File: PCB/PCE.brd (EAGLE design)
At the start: 58.5 x 61 mm, 13 parts, among them U1 SN74AHCT125N, U2 SN74AHCT125N

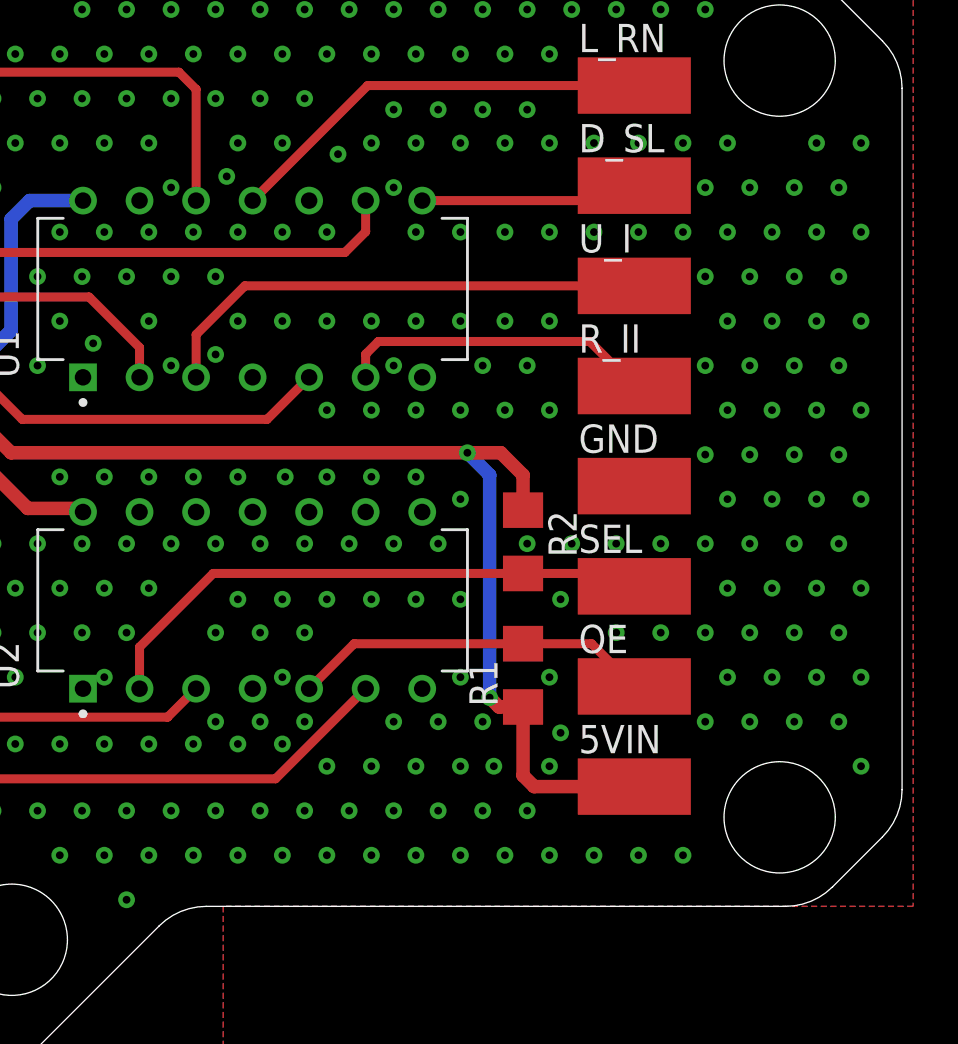
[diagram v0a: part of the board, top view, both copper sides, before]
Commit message: PCB Updates/New Additions
All existing PCBs had silkscreen updates and NES, Virtual Boy, PSX/PS2, Nintendo 64, Saturn have been added.
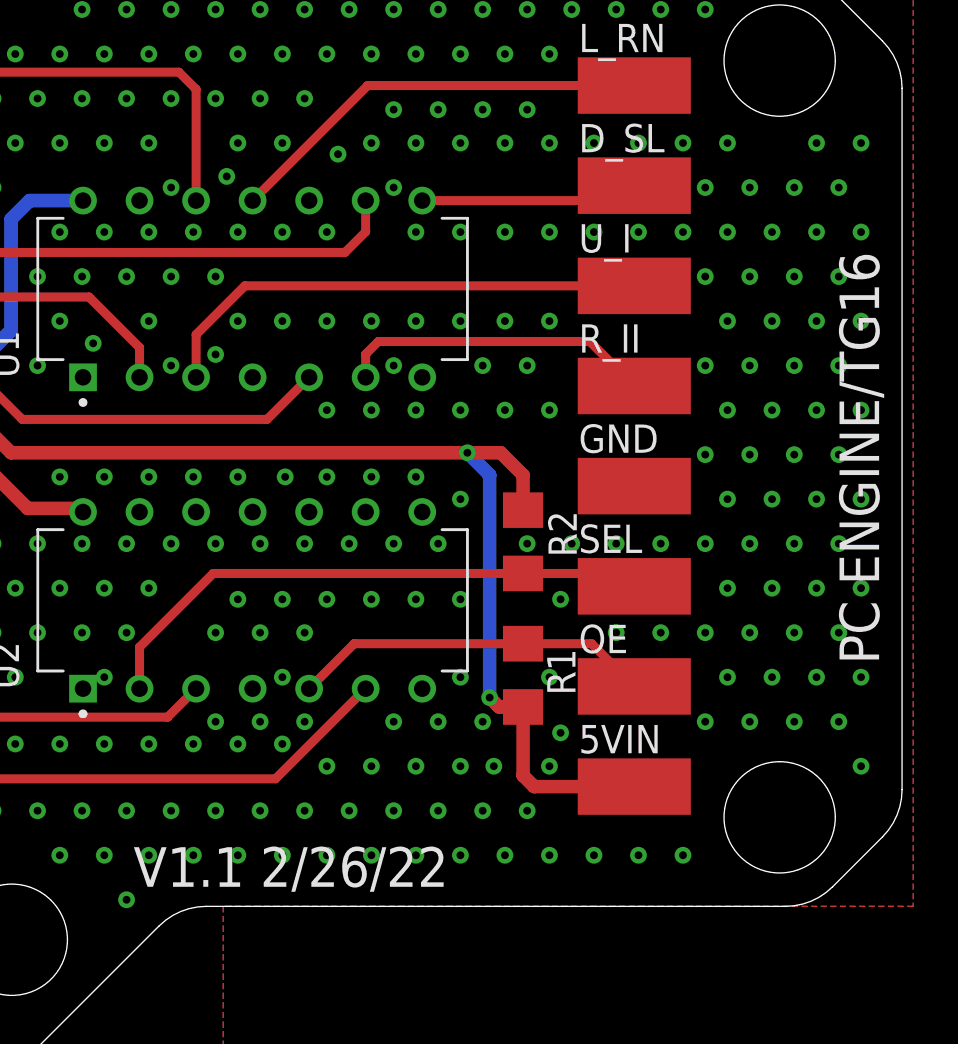
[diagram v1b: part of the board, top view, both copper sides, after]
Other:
- board text added: "PC ENGINE/TG16"
- board text added: "V1.1 2/26/22"
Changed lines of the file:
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@@
 <drawing>
 <settings>
-<setting alwaysvectorfont="no"/>
+<setting alwaysvectorfont="yes"/>
 <setting verticaltext="up"/>
 </settings>
@@
 <hole x="18.53" y="53.12" drill="5"/>
 <hole x="18.53" y="8.12" drill="5"/>
+<text x="57.5" y="20.5" size="1.778" layer="21" rot="R90">PC ENGINE/TG16</text>
+<text x="24" y="10.5" size="1.778" layer="21">V1.1 2/26/22</text>
 </plain>
 <attributes>
@@
 <element name="R2" library="adafruit" library_urn="urn:adsk.eagle:library:420" package="R1206" package3d_urn="urn:adsk.eagle:package:6240569/1" value="47k" x="41.5" y="26" smashed="yes" rot="R270">
 <attribute name="NAME" x="42.643" y="27.397" size="1.27" layer="25" rot="R270"/>
-<attribute name="VALUE" x="39.087" y="27.397" size="1.27" layer="27" rot="R270"/>
 </element>
 <element name="R1" library="adafruit" library_urn="urn:adsk.eagle:library:420" package="R1206" package3d_urn="urn:adsk.eagle:package:6240569/1" value="47k" x="41.5" y="20" smashed="yes" rot="R90">
-<attribute name="NAME" x="40.357" y="18.603" size="1.27" layer="25" rot="R90"/>
-<attribute name="VALUE" x="43.913" y="16.603" size="1.27" layer="27" rot="R90"/>
+<attribute name="NAME" x="43.857" y="19.103" size="1.27" layer="25" rot="R90"/>
 </element>
 <element name="U2" library="SN74AHCT125N" package="DIP794W45P254L1969H508Q14" value="SN74AHCT125N" x="29.35" y="23.37" smashed="yes" rot="R90">
@@
 <attribute name="PRICE" value="None" x="150" y="47.5" size="1.778" layer="27" rot="R90" display="off"/>
 <attribute name="PURCHASE-URL" value="https://pricing.snapeda.com/search/part/SN74AHCT125N/?ref=eda" x="150" y="47.5" size="1.778" layer="27" rot="R90" display="off"/>
-<attribute name="VALUE" x="39.85" y="19.37" size="1.27" layer="27" rot="R90" align="top-left"/>
 </element>
 <element name="U1" library="SN74AHCT125N" package="DIP794W45P254L1969H508Q14" value="SN74AHCT125N" x="29.35" y="37.36" smashed="yes" rot="R90">
@@
 <attribute name="PRICE" value="None" x="150" y="78" size="1.778" layer="27" rot="R90" display="off"/>
 <attribute name="PURCHASE-URL" value="https://pricing.snapeda.com/search/part/SN74AHCT125N/?ref=eda" x="150" y="78" size="1.778" layer="27" rot="R90" display="off"/>
-<attribute name="VALUE" x="39.85" y="33.36" size="1.27" layer="27" rot="R90" align="top-left"/>
 </element>
 <element name="X1" library="SparkFun-Retired" package="F25H" value="" x="10.67" y="30.54" smashed="yes" rot="R90">

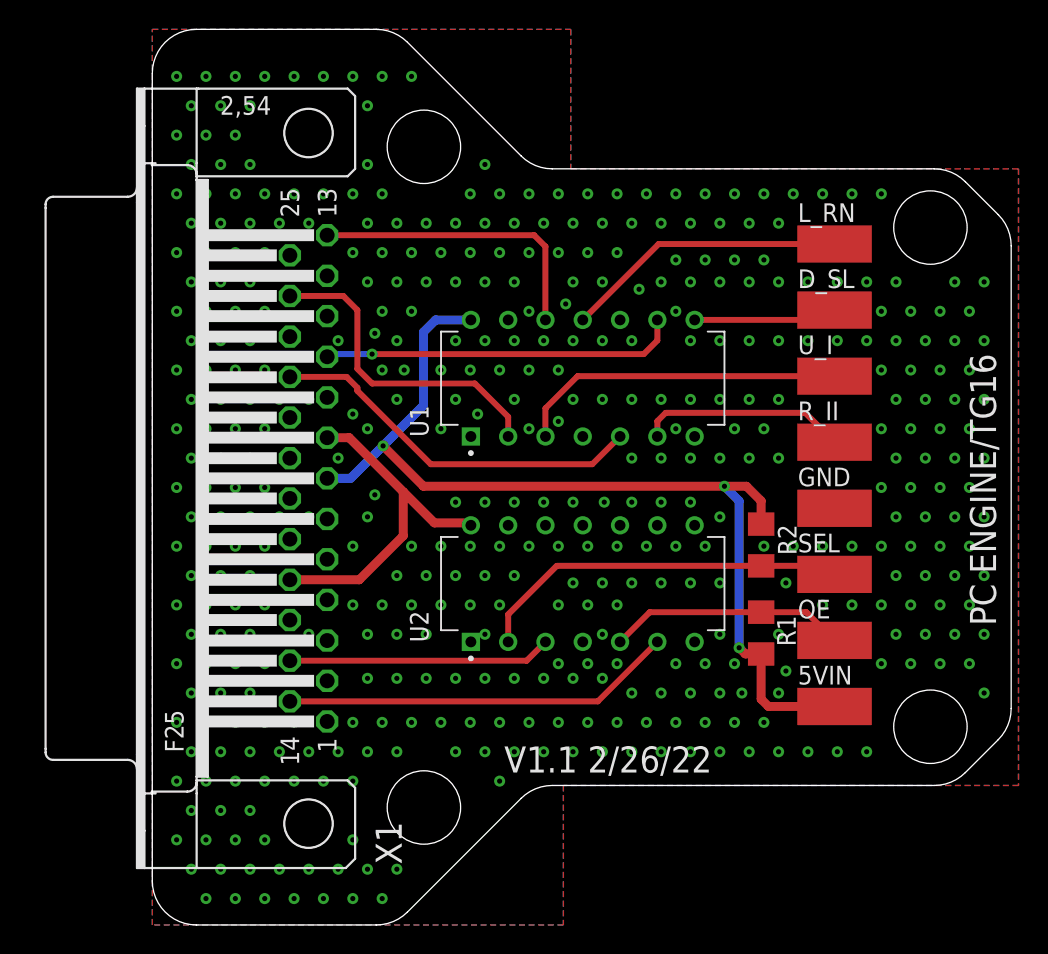
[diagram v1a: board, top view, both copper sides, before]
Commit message: PCB Update for better Housing Fit
All the PCBs were updated for better housing fitment.

Common Changes across all PCBs:
1. All Aux PCBs are now the exact same size.  (there was a .1mm-.5mm Variance previous)
2. All Aux PCBs Mounting holes are in the same location (there was a .05mm-.1mm Variance previous)
3. The DB25 has been moved 1.2mm close to the edge of the PCB for better connection when in the housing.

PCB Specific Updates:
3DO - Rename Pads (Removed trailing numbers), Flipped U2 to match U1, Moved U1 & U2 to same coordinates as other 2 Component PCBs in collection.

PCE & NES- Moved U1 & U2 to same coordinates as other 2 Component PCBs in collection.

PS2/PSX & Saturn - Added Notch on back edge of PCB for access for wires that need to attach to bottom layer of PCB.

All Gerbers have been updated.

New PCBs have been ordered for testing.
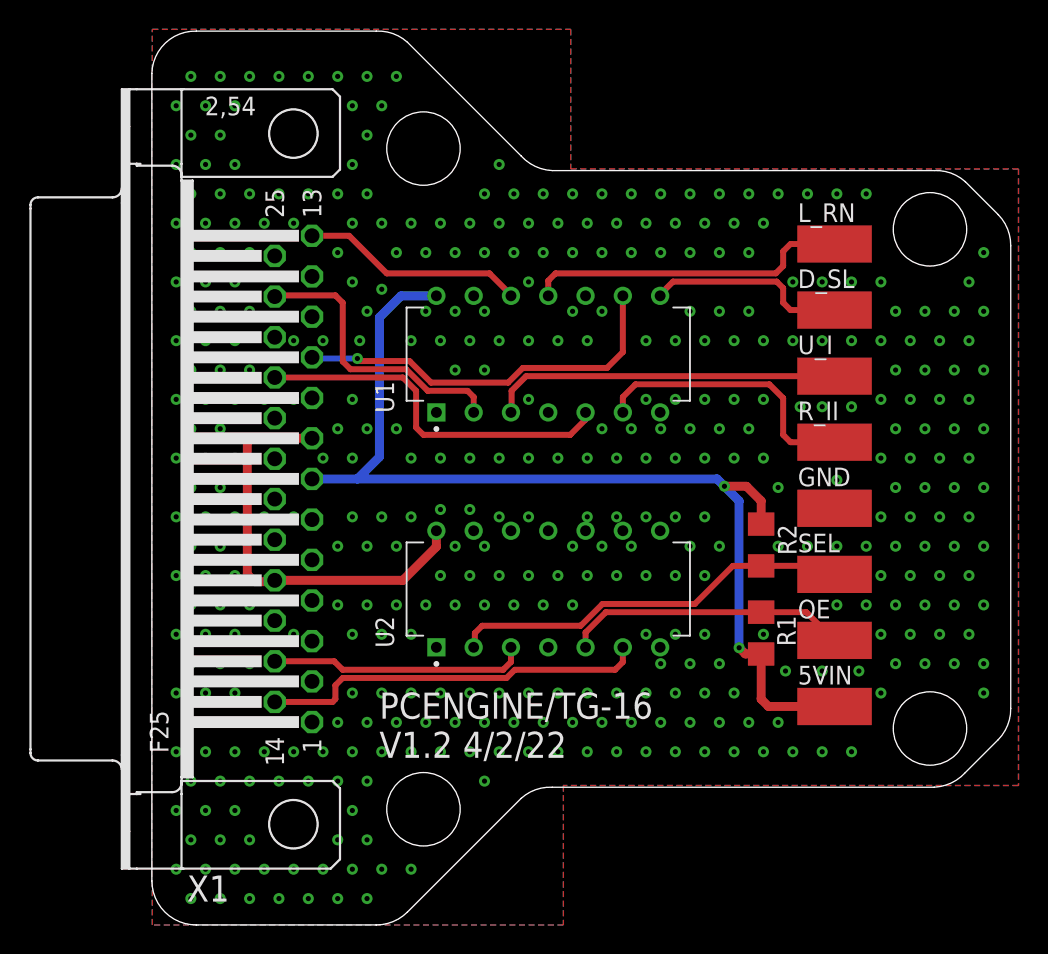
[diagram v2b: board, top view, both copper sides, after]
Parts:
- moved U1 2.87 mm to (27.0, 39.0)
- moved U2 2.38 mm to (27.0, 23.0)
- moved X1 1.03 mm to (9.64, 30.5)
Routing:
- net IO23: track 20.2 -> 15.3 mm
- net R_II: track 14.2 -> 18.9 mm
- net 3V3IN: track 24.2 -> 28.7 mm
- net D_SL: track 9.81 -> 13.7 mm
- net OE: track 16.2 -> 19.3 mm
- net L_RN: track 19.3 -> 22.2 mm
- net 5VIN: track 67.4 -> 70.3 mm, vias 3 -> 2
- net IO18: track 24.3 -> 26.6 mm
- net IO3: track 22.0 -> 19.8 mm
- net SEL: track 25.7 -> 27.6 mm
- net U_I: track 22.5 -> 23.9 mm
- net IO5: track 25.9 -> 25.2 mm
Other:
- board size 58.5 x 61 mm -> 58.5 x 60.9 mm
- board text added: "PCENGINE/TG-16 V1.2 4/2/22"
- board text removed: "PC ENGINE/TG16"
- board text removed: "V1.1 2/26/22"
